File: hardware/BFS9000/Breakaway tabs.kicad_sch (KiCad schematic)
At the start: 34 parts

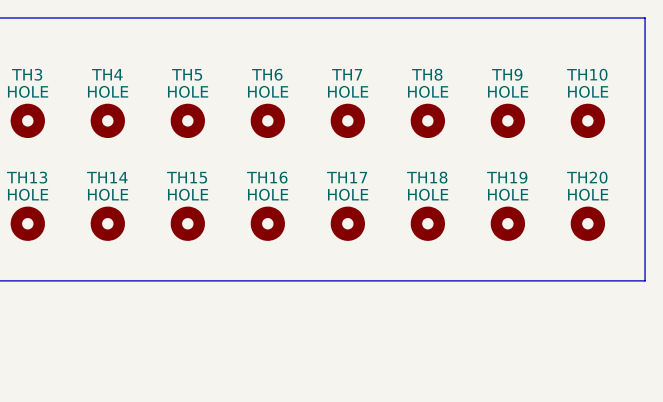
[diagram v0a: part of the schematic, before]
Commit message: feat(hardware): add RP2040 footprint and peripheral circuitry
Add the RP2040 footprint, decoupling capacitors, OLED connectors, I2C pull-up resistors, and left/right keyboard side detection circuitry.
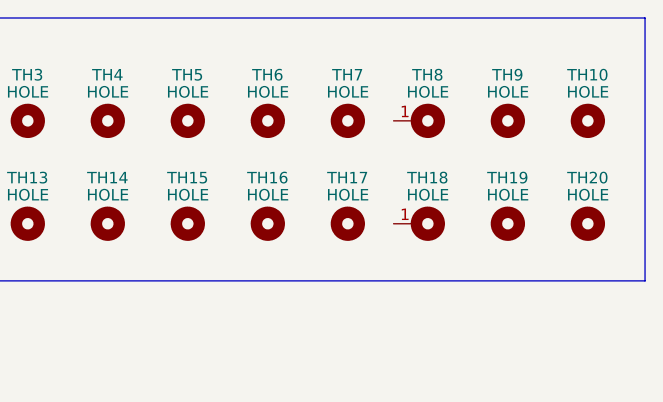
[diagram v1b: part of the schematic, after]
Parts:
- TH1, TH17: footprint BFS9000:Tenting_Puck.kicad_mod_nocenter_v2 -> BFS9000:Hole from sofle for M2 posts gold rimmer wide-keyplate-hole
- TH18, TH8: footprint BFS9000:Hole from sofle for M2 posts gold rimmer wide-keyplate-hole -> BFS9000:Tenting_Puck.kicad_mod_nocenter_v2
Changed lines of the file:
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@@
 	(title_block
 		(title "BSF9000")
-		(date "2026-05-01")
+		(date "2026-05-03")
 		(rev "0.3")
 		(company "jguillen-lab")
@@
 			)
 		)
-		(property "Footprint" "BFS9000:Tenting_Puck.kicad_mod_nocenter_v2"
+		(property "Footprint" "BFS9000:Hole from sofle for M2 posts gold rimmer wide-keyplate-hole"
 			(at 189.23 30.48 0)
 			(hide yes)
@@
 			)
 		)
-		(property "Footprint" "BFS9000:Tenting_Puck.kicad_mod_nocenter_v2"
+		(property "Footprint" "BFS9000:Hole from sofle for M2 posts gold rimmer wide-keyplate-hole"
 			(at 243.84 41.91 0)
 			(hide yes)
@@
 	)
 	(symbol
+		(lib_name "MountingHole_2")
 		(lib_id "BFS9000:MountingHole")
 		(at 252.73 41.91 0)
@@
 			)
 		)
-		(property "Footprint" "BFS9000:Hole from sofle for M2 posts gold rimmer wide-keyplate-hole"
+		(property "Footprint" "BFS9000:Tenting_Puck.kicad_mod_nocenter_v2"
 			(at 252.73 41.91 0)
 			(hide yes)
@@
 			)
 		)
+		(pin "1"
+		)
 		(instances
 			(project "BFS9000"
@@
 	)
 	(symbol
+		(lib_name "MountingHole_1")
 		(lib_id "BFS9000:MountingHole")
 		(at 252.73 30.48 0)
@@
 			)
 		)
-		(property "Footprint" "BFS9000:Hole from sofle for M2 posts gold rimmer wide-keyplate-hole"
+		(property "Footprint" "BFS9000:Tenting_Puck.kicad_mod_nocenter_v2"
 			(at 252.73 30.48 0)
 			(hide yes)
@@
 			)
 		)
+		(pin "1"
+		)
 		(instances

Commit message: feat(hardware): integrate RGB and switch matrix layout
Add dedicated schematic sheets for addressable RGB LEDs and keyboard switches.

Place SK6803 MINI-E LEDs, MX switch footprints, stabilizers, rotary encoder, jack connector, and related power/control components in the BFS9000 PCB layout.

Update the main schematic, project settings, and breakaway tabs sheet to match the expanded hardware design.
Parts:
- TH1, TH2, TH4, TH5: footprint BFS9000:Hole from sofle for M2 posts gold rimmer wide-keyplate-hole -> BFS9000:Hole from sofle for M2 posts gold rimmer narrow-keyplate-hole
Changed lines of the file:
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@@
 	(title_block
 		(title "BSF9000")
-		(date "2026-05-03")
+		(date "2026-05-01")
 		(rev "0.3")
 		(company "jguillen-lab")
@@
 			)
 		)
-		(property "Footprint" "BFS9000:Hole from sofle for M2 posts gold rimmer wide-keyplate-hole"
+		(property "Footprint" "BFS9000:Hole from sofle for M2 posts gold rimmer narrow-keyplate-hole"
 			(at 189.23 30.48 0)
 			(hide yes)
@@
 			)
 		)
-		(property "Footprint" "BFS9000:Hole from sofle for M2 posts gold rimmer wide-keyplate-hole"
+		(property "Footprint" "BFS9000:Hole from sofle for M2 posts gold rimmer narrow-keyplate-hole"
 			(at 199.39 30.48 0)
 			(hide yes)
@@
 			)
 		)
-		(property "Footprint" "BFS9000:Hole from sofle for M2 posts gold rimmer wide-keyplate-hole"
+		(property "Footprint" "BFS9000:Hole from sofle for M2 posts gold rimmer narrow-keyplate-hole"
 			(at 226.06 30.48 0)
 			(hide yes)
@@
 			)
 		)
-		(property "Footprint" "BFS9000:Hole from sofle for M2 posts gold rimmer wide-keyplate-hole"
+		(property "Footprint" "BFS9000:Hole from sofle for M2 posts gold rimmer narrow-keyplate-hole"
 			(at 217.17 30.48 0)
 			(hide yes)

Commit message: feat(hardware): update BFS9000 schematic and PCB layout
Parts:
- Cut_1, Cut_10, Cut_11, Cut_12, Cut_13, Cut_14, Cut_2, Cut_3, Cut_4, Cut_5, Cut_6, Cut_7, Cut_8, Cut_9: footprint BFS9000:LongOvalCut -> BFS9000:Cutout_Long_Oval; symbol Mechanical:MountingHole -> BFS9000:MountingHole
- TH1, TH2, TH4, TH5: footprint BFS9000:Hole from sofle for M2 posts gold rimmer narrow-keyplate-hole -> BFS9000:Mount_M2_Post_Hole_Keyplate_Narrow
- TH10, TH11, TH12, TH13, TH14, TH15, TH16, TH17, TH19, TH20, TH3, TH6, TH7, TH9: footprint BFS9000:Hole from sofle for M2 posts gold rimmer wide-keyplate-hole -> BFS9000:Mount_M2_Post_Hole_Keyplate_Wide
- TH18, TH8: footprint BFS9000:Tenting_Puck.kicad_mod_nocenter_v2 -> BFS9000:Mount_Tenting_Puck
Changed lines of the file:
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@@
 	(generator "eeschema")
 	(generator_version "10.0")
-	(paper "A4")
+	(paper "A3")
 	(title_block
 		(title "BSF9000")
@@
 			)
 		)
-		(property "Footprint" "BFS9000:Hole from sofle for M2 posts gold rimmer narrow-keyplate-hole"
+		(property "Footprint" "BFS9000:Mount_M2_Post_Hole_Keyplate_Narrow"
 			(at 189.23 30.48 0)
 			(hide yes)
@@
 			)
 		)
-		(property "Footprint" "BFS9000:Hole from sofle for M2 posts gold rimmer narrow-keyplate-hole"
+		(property "Footprint" "BFS9000:Mount_M2_Post_Hole_Keyplate_Narrow"
 			(at 199.39 30.48 0)
 			(hide yes)
@@
 			)
 		)
-		(property "Footprint" "BFS9000:Hole from sofle for M2 posts gold rimmer wide-keyplate-hole"
+		(property "Footprint" "BFS9000:Mount_M2_Post_Hole_Keyplate_Wide"
 			(at 208.28 41.91 0)
 			(hide yes)
@@
 			)
 		)
-		(property "Footprint" "BFS9000:Hole from sofle for M2 posts gold rimmer wide-keyplate-hole"
+		(property "Footprint" "BFS9000:Mount_M2_Post_Hole_Keyplate_Wide"
 			(at 208.28 30.48 0)
 			(hide yes)
@@
 			)
 		)
-		(property "Footprint" "BFS9000:Hole from sofle for M2 posts gold rimmer narrow-keyplate-hole"
+		(property "Footprint" "BFS9000:Mount_M2_Post_Hole_Keyplate_Narrow"
 			(at 226.06 30.48 0)
 			(hide yes)
@@
 			)
 		)
-		(property "Footprint" "BFS9000:Hole from sofle for M2 posts gold rimmer wide-keyplate-hole"
+		(property "Footprint" "BFS9000:Mount_M2_Post_Hole_Keyplate_Wide"
 			(at 189.23 41.91 0)
 			(hide yes)
@@
 	)
 	(symbol
-		(lib_id "Mechanical:MountingHole")
+		(lib_id "BFS9000:MountingHole")
 		(at 27.94 27.94 0)
 		(unit 1)
@@
 			)
 		)
-		(property "Footprint" "BFS9000:LongOvalCut"
+		(property "Footprint" "BFS9000:Cutout_Long_Oval"
 			(at 27.94 27.94 0)
 			(hide yes)
@@
 	)
 	(symbol
-		(lib_id "Mechanical:MountingHole")
+		(lib_id "BFS9000:MountingHole")
 		(at 80.01 35.56 0)
 		(unit 1)
@@
 			)
 		)
-		(property "Footprint" "BFS9000:LongOvalCut"
+		(property "Footprint" "BFS9000:Cutout_Long_Oval"
 			(at 80.01 35.56 0)
 			(hide yes)
@@
 			)
 		)
-		(property "Footprint" "BFS9000:Hole from sofle for M2 posts gold rimmer wide-keyplate-hole"
+		(property "Footprint" "BFS9000:Mount_M2_Post_Hole_Keyplate_Wide"
 			(at 270.51 41.91 0)
 			(hide yes)
@@
 			)
 		)
-		(property "Footprint" "BFS9000:Hole from sofle for M2 posts gold rimmer wide-keyplate-hole"
+		(property "Footprint" "BFS9000:Mount_M2_Post_Hole_Keyplate_Wide"
 			(at 234.95 30.48 0)
 			(hide yes)
@@
 	)
 	(symbol
-		(lib_id "Mechanical:MountingHole")
+		(lib_id "BFS9000:MountingHole")
 		(at 27.94 43.18 0)
 		(unit 1)
@@
 			)
 		)
-		(property "Footprint" "BFS9000:LongOvalCut"
+		(property "Footprint" "BFS9000:Cutout_Long_Oval"
 			(at 27.94 43.18 0)
 			(hide yes)
@@
 	)
 	(symbol
-		(lib_id "Mechanical:MountingHole")
+		(lib_id "BFS9000:MountingHole")
 		(at 54.61 43.18 0)
 		(unit 1)
@@
 			)
 		)
-		(property "Footprint" "BFS9000:LongOvalCut"
+		(property "Footprint" "BFS9000:Cutout_Long_Oval"
 			(at 54.61 43.18 0)
 			(hide yes)
@@
 			)
 		)
-		(property "Footprint" "BFS9000:Hole from sofle for M2 posts gold rimmer wide-keyplate-hole"
+		(property "Footprint" "BFS9000:Mount_M2_Post_Hole_Keyplate_Wide"
 			(at 243.84 41.91 0)
 			(hide yes)
@@
 	)
 	(symbol
-		(lib_id "Mechanical:MountingHole")
+		(lib_id "BFS9000:MountingHole")
 		(at 80.01 27.94 0)
 		(unit 1)
@@
 			)
 		)
-		(property "Footprint" "BFS9000:LongOvalCut"
+		(property "Footprint" "BFS9000:Cutout_Long_Oval"
 			(at 80.01 27.94 0)
 			(hide yes)
@@
 			)
 		)
-		(property "Footprint" "BFS9000:Hole from sofle for M2 posts gold rimmer wide-keyplate-hole"
+		(property "Footprint" "BFS9000:Mount_M2_Post_Hole_Keyplate_Wide"
 			(at 226.06 41.91 0)
 			(hide yes)
@@
 			)
 		)
-		(property "Footprint" "BFS9000:Hole from sofle for M2 posts gold rimmer wide-keyplate-hole"
+		(property "Footprint" "BFS9000:Mount_M2_Post_Hole_Keyplate_Wide"
 			(at 270.51 30.48 0)
 			(hide yes)
@@
 			)
 		)
-		(property "Footprint" "BFS9000:Tenting_Puck.kicad_mod_nocenter_v2"
+		(property "Footprint" "BFS9000:Mount_Tenting_Puck"
 			(at 252.73 41.91 0)
 			(hide yes)
@@
 			)
 		)
-		(property "Footprint" "BFS9000:Hole from sofle for M2 posts gold rimmer wide-keyplate-hole"
+		(property "Footprint" "BFS9000:Mount_M2_Post_Hole_Keyplate_Wide"
 			(at 261.62 41.91 0)
 			(hide yes)
@@
 			)
 		)
-		(property "Footprint" "BFS9000:Hole from sofle for M2 posts gold rimmer wide-keyplate-hole"
+		(property "Footprint" "BFS9000:Mount_M2_Post_Hole_Keyplate_Wide"
 			(at 217.17 41.91 0)
 			(hide yes)
@@
 	)
 	(symbol
-		(lib_id "Mechanical:MountingHole")
+		(lib_id "BFS9000:MountingHole")
 		(at 54.61 35.56 0)
 		(unit 1)
@@
 			)
 		)
-		(property "Footprint" "BFS9000:LongOvalCut"
+		(property "Footprint" "BFS9000:Cutout_Long_Oval"
 			(at 54.61 35.56 0)
 			(hide yes)
@@
 			)
 		)
-		(property "Footprint" "BFS9000:Hole from sofle for M2 posts gold rimmer wide-keyplate-hole"
+		(property "Footprint" "BFS9000:Mount_M2_Post_Hole_Keyplate_Wide"
 			(at 243.84 30.48 0)
 			(hide yes)
@@
 	)
 	(symbol
-		(lib_id "Mechanical:MountingHole")
+		(lib_id "BFS9000:MountingHole")
 		(at 54.61 27.94 0)
 		(unit 1)
@@
 			)
 		)
-		(property "Footprint" "BFS9000:LongOvalCut"
+		(property "Footprint" "BFS9000:Cutout_Long_Oval"
 			(at 54.61 27.94 0)
 			(hide yes)
@@
 	)
 	(symbol
-		(lib_id "Mechanical:MountingHole")
+		(lib_id "BFS9000:MountingHole")
 		(at 54.61 50.8 0)
 		(unit 1)
@@
 			)
 		)
-		(property "Footprint" "BFS9000:LongOvalCut"
+		(property "Footprint" "BFS9000:Cutout_Long_Oval"
 			(at 54.61 50.8 0)
 			(hide yes)
@@
 	)
 	(symbol
-		(lib_id "Mechanical:MountingHole")
+		(lib_id "BFS9000:MountingHole")
 		(at 80.01 43.18 0)
 		(unit 1)
@@
 			)
 		)
-		(property "Footprint" "BFS9000:LongOvalCut"
+		(property "Footprint" "BFS9000:Cutout_Long_Oval"
 			(at 80.01 43.18 0)
 			(hide yes)
@@
 			)
 		)
-		(property "Footprint" "BFS9000:Hole from sofle for M2 posts gold rimmer narrow-keyplate-hole"
+		(property "Footprint" "BFS9000:Mount_M2_Post_Hole_Keyplate_Narrow"
 			(at 217.17 30.48 0)
 			(hide yes)
@@
 	)
 	(symbol
-		(lib_id "Mechanical:MountingHole")
+		(lib_id "BFS9000:MountingHole")
 		(at 105.41 43.18 0)
 		(unit 1)
@@
 			)
 		)
-		(property "Footprint" "BFS9000:LongOvalCut"
+		(property "Footprint" "BFS9000:Cutout_Long_Oval"
 			(at 105.41 43.18 0)
 			(hide yes)
@@
 	)
 	(symbol
-		(lib_id "Mechanical:MountingHole")
+		(lib_id "BFS9000:MountingHole")
 		(at 105.41 27.94 0)
 		(unit 1)
@@
 			)
 		)
-		(property "Footprint" "BFS9000:LongOvalCut"
+		(property "Footprint" "BFS9000:Cutout_Long_Oval"
 			(at 105.41 27.94 0)
 			(hide yes)
@@
 	)
 	(symbol
-		(lib_id "Mechanical:MountingHole")
+		(lib_id "BFS9000:MountingHole")
 		(at 27.94 50.8 0)
 		(unit 1)
@@
 			)
 		)
-		(property "Footprint" "BFS9000:LongOvalCut"
+		(property "Footprint" "BFS9000:Cutout_Long_Oval"
 			(at 27.94 50.8 0)
 			(hide yes)
@@
 			)
 		)
-		(property "Footprint" "BFS9000:Hole from sofle for M2 posts gold rimmer wide-keyplate-hole"
+		(property "Footprint" "BFS9000:Mount_M2_Post_Hole_Keyplate_Wide"
 			(at 234.95 41.91 0)
 			(hide yes)
@@
 			)
 		)
-		(property "Footprint" "BFS9000:Hole from sofle for M2 posts gold rimmer wide-keyplate-hole"
+		(property "Footprint" "BFS9000:Mount_M2_Post_Hole_Keyplate_Wide"
 			(at 199.39 41.91 0)
 			(hide yes)
@@
 	)
 	(symbol
-		(lib_id "Mechanical:MountingHole")
+		(lib_id "BFS9000:MountingHole")
 		(at 27.94 35.56 0)
 		(unit 1)
@@
 			)
 		)
-		(property "Footprint" "BFS9000:LongOvalCut"
+		(property "Footprint" "BFS9000:Cutout_Long_Oval"
 			(at 27.94 35.56 0)
 			(hide yes)
@@
 	)
 	(symbol
-		(lib_id "Mechanical:MountingHole")
+		(lib_id "BFS9000:MountingHole")
 		(at 105.41 35.56 0)
 		(unit 1)
@@
 			)
 		)
-		(property "Footprint" "BFS9000:LongOvalCut"
+		(property "Footprint" "BFS9000:Cutout_Long_Oval"
 			(at 105.41 35.56 0)
 			(hide yes)
@@
 			)
 		)
-		(property "Footprint" "BFS9000:Tenting_Puck.kicad_mod_nocenter_v2"
+		(property "Footprint" "BFS9000:Mount_Tenting_Puck"
 			(at 252.73 30.48 0)
 			(hide yes)
@@
 			)
 		)
-		(property "Footprint" "BFS9000:Hole from sofle for M2 posts gold rimmer wide-keyplate-hole"
+		(property "Footprint" "BFS9000:Mount_M2_Post_Hole_Keyplate_Wide"
 			(at 261.62 30.48 0)
 			(hide yes)
